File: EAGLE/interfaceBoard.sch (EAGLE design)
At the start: 7 parts, among them SW1 EC12E_SW

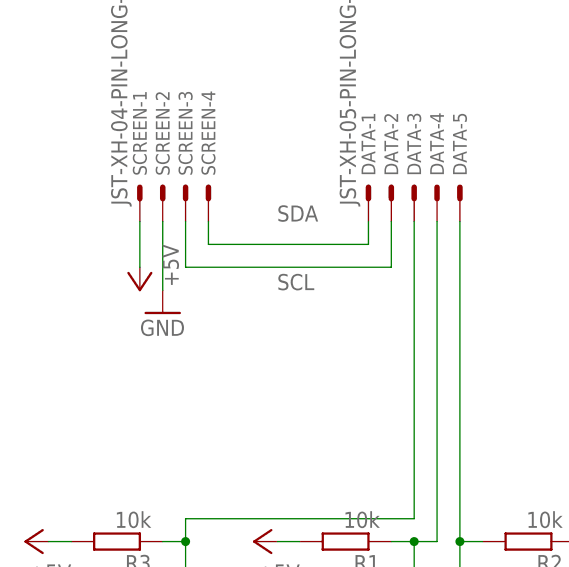
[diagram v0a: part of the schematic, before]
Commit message: * Small fix where the +5v and GND rail was reversed to the LCD screen on the interface board
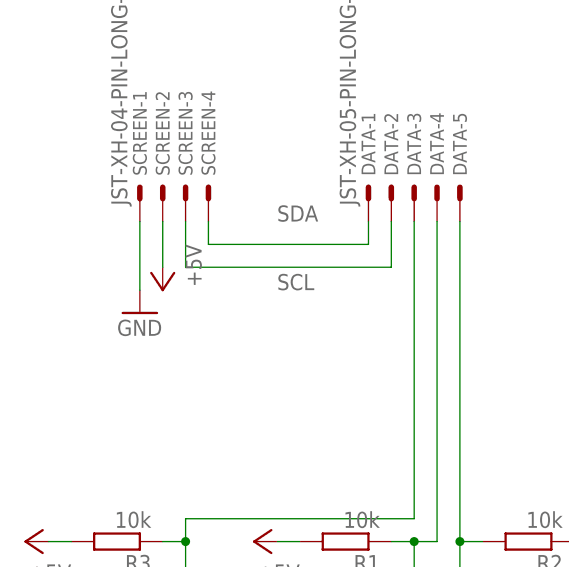
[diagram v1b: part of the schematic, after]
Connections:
- net +5V: now also SCREEN-2.S; no longer SCREEN-1.S
- net GND: now also SCREEN-1.S; no longer SCREEN-2.S
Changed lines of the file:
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@@
 <attribute name="VALUE" x="38.1" y="30.48" size="1.778" layer="96"/>
 </instance>
-<instance part="GND4" gate="1" x="38.1" y="78.74" smashed="yes">
-<attribute name="VALUE" x="35.56" y="76.2" size="1.778" layer="96"/>
+<instance part="GND4" gate="1" x="35.56" y="78.74" smashed="yes">
+<attribute name="VALUE" x="33.02" y="76.2" size="1.778" layer="96"/>
 </instance>
-<instance part="P+5" gate="1" x="35.56" y="81.28" smashed="yes" rot="R180">
-<attribute name="VALUE" x="38.1" y="86.36" size="1.778" layer="96" rot="R270"/>
+<instance part="P+5" gate="1" x="38.1" y="81.28" smashed="yes" rot="R180">
+<attribute name="VALUE" x="40.64" y="86.36" size="1.778" layer="96" rot="R270"/>
 </instance>
 </instances>
@@
 </segment>
 <segment>
-<pinref part="SCREEN" gate="-2" pin="S"/>
+<pinref part="SCREEN" gate="-1" pin="S"/>
 <pinref part="GND4" gate="1" pin="GND"/>
-<wire x1="38.1" y1="88.9" x2="38.1" y2="81.28" width="0.1524" layer="91"/>
+<wire x1="35.56" y1="88.9" x2="35.56" y2="81.28" width="0.1524" layer="91"/>
 </segment>
 </net>
@@
 </segment>
 <segment>
-<pinref part="SCREEN" gate="-1" pin="S"/>
 <pinref part="P+5" gate="1" pin="+5V"/>
-<wire x1="35.56" y1="88.9" x2="35.56" y2="83.82" width="0.1524" layer="91"/>
+<pinref part="SCREEN" gate="-2" pin="S"/>
+<wire x1="38.1" y1="83.82" x2="38.1" y2="88.9" width="0.1524" layer="91"/>
 </segment>
 </net>
